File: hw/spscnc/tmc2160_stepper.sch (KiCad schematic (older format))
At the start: 65 parts, among them IC1 TMC2160-TA, Q13 KIA50N06B, Q14 KIA50N06B, Q15 KIA50N06B, Q5 KIA50N06B, Q6 KIA50N06B, Q7 KIA50N06B, Q8 KIA50N06B, Q9 KIA50N06B

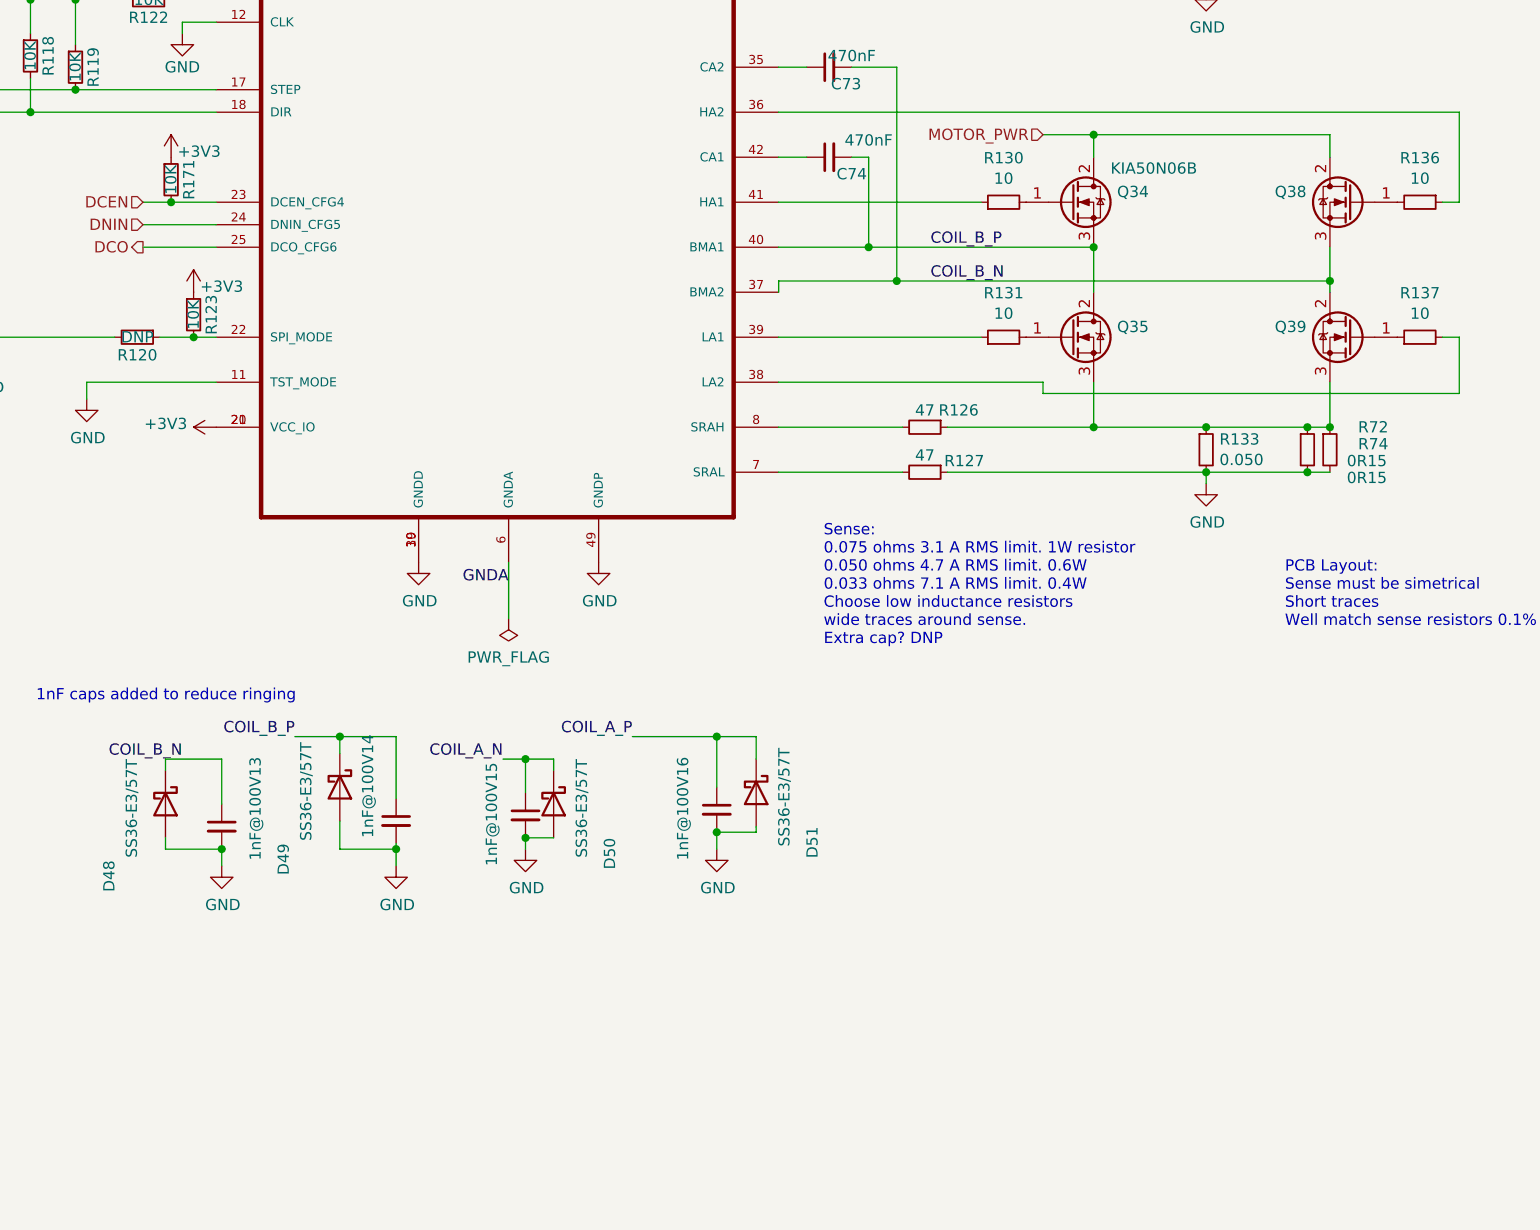
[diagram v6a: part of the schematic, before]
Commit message: Prototype corrections without new PCB
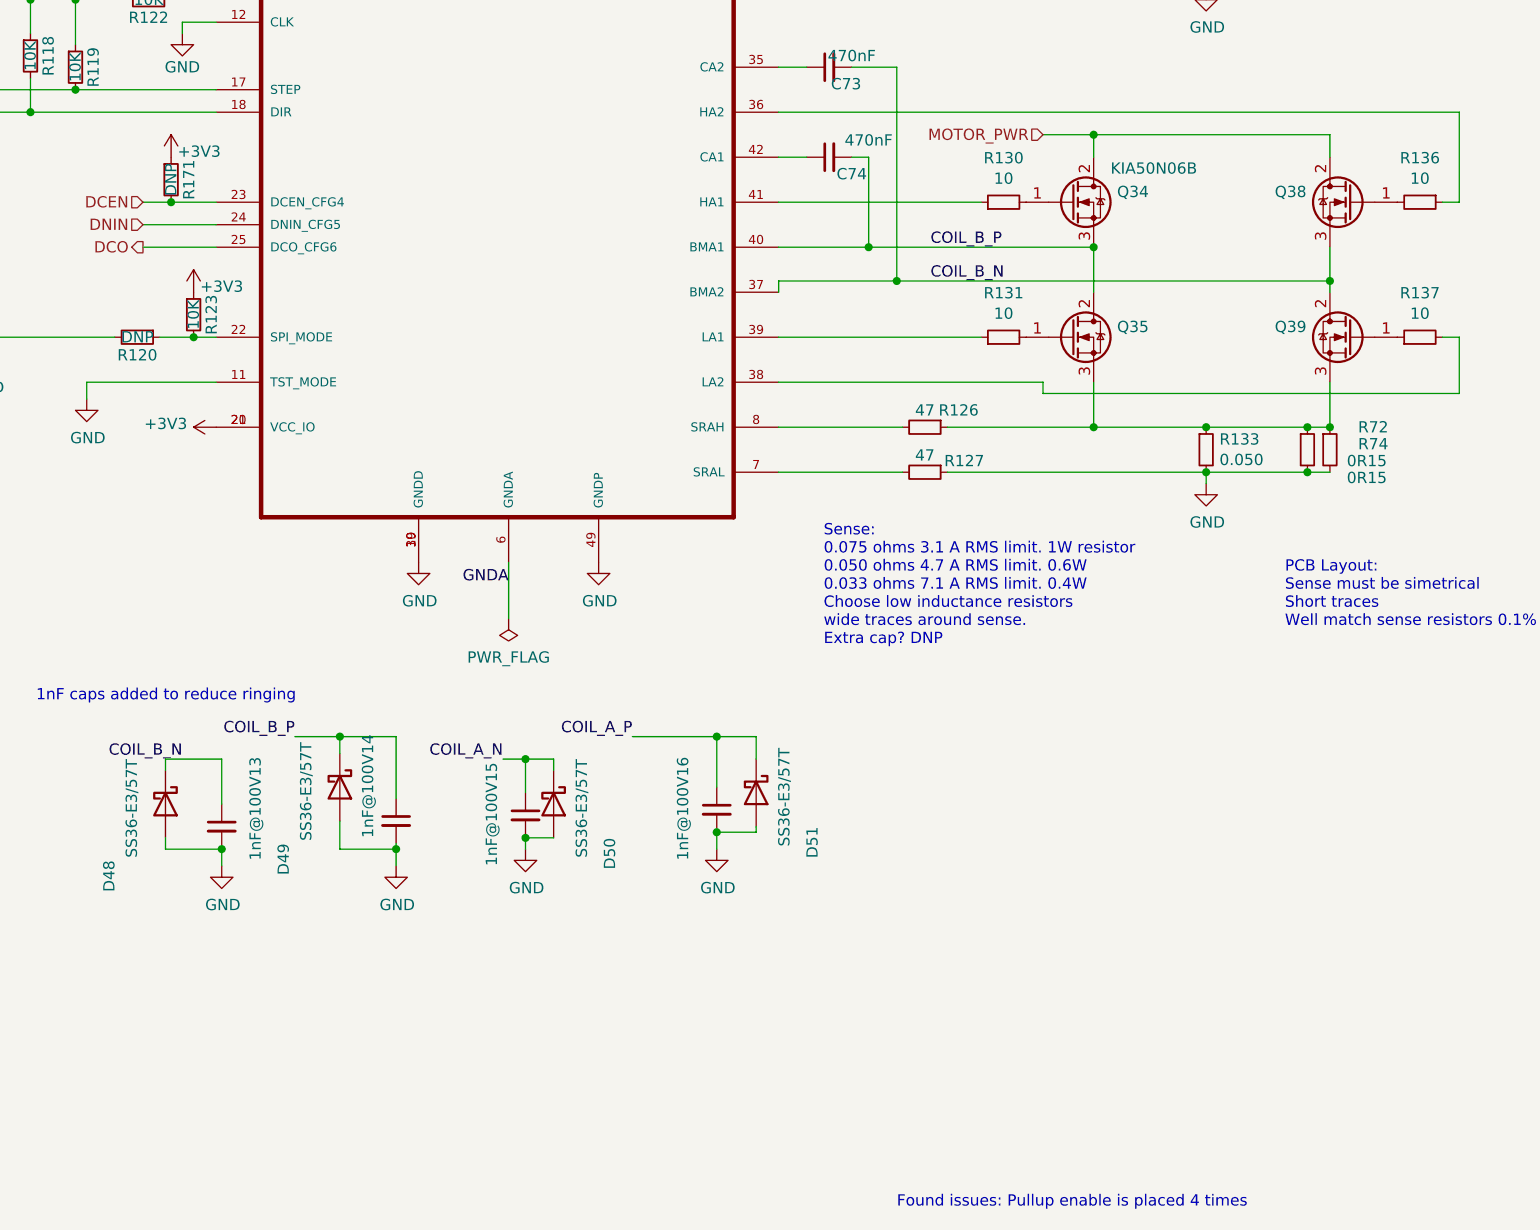
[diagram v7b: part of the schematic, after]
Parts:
- R168: value 10K -> DNP; jlcpcb C17414 -> DNP734
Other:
- note added: "Found issues: Pullup enable is placed 4 times"
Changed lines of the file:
@@
 AR Path="/61E6E495" Ref="#PWR0103"  Part="1"
 AR Path="/6221509B/61E6E495" Ref="#PWR?"  Part="1"
-F 0 "#PWR065" H 1875 1825 50  0001 C CNN
+F 0 "#PWR085" H 1875 1825 50  0001 C CNN
 F 1 "GND" H 1880 1902 50  0000 C CNN
 F 2 "" H 1875 2075 50  0001 C CNN
@@
 AR Path="/61E77854" Ref="#PWR0104"  Part="1"
 AR Path="/6221509B/61E77854" Ref="#PWR?"  Part="1"
-F 0 "#PWR076" H 7050 800 50  0001 C CNN
+F 0 "#PWR096" H 7050 800 50  0001 C CNN
 F 1 "GND" H 7055 877 50  0000 C CNN
 F 2 "" H 7050 1050 50  0001 C CNN
@@
 AR Path="/61E77EC9" Ref="#PWR0105"  Part="1"
 AR Path="/6221509B/61E77EC9" Ref="#PWR?"  Part="1"
-F 0 "#PWR080" H 8525 800 50  0001 C CNN
+F 0 "#PWR0100" H 8525 800 50  0001 C CNN
 F 1 "GND" H 8530 877 50  0000 C CNN
 F 2 "" H 8525 1050 50  0001 C CNN
@@
 AR Path="/6203DFCF/61E7935F" Ref="#PWR091"  Part="1"
 AR Path="/6221509B/61E7935F" Ref="#PWR?"  Part="1"
-F 0 "#PWR071" H 3500 5125 50  0001 C CNN
+F 0 "#PWR091" H 3500 5125 50  0001 C CNN
 F 1 "+3V3" V 3515 5403 50  0000 L CNN
 F 2 "" H 3500 5275 50  0001 C CNN
@@
 AR Path="/61E79E80" Ref="#PWR0110"  Part="1"
 AR Path="/6221509B/61E79E80" Ref="#PWR?"  Part="1"
-F 0 "#PWR064" H 1875 1325 50  0001 C CNN
+F 0 "#PWR084" H 1875 1325 50  0001 C CNN
 F 1 "+12V" H 1890 1648 50  0000 C CNN
 F 2 "" H 1875 1475 50  0001 C CNN
@@
 AR Path="/61E86B21" Ref="#PWR0115"  Part="1"
 AR Path="/6221509B/61E86B21" Ref="#PWR?"  Part="1"
-F 0 "#PWR072" H 4400 5625 50  0001 C CNN
+F 0 "#PWR092" H 4400 5625 50  0001 C CNN
 F 1 "GND" H 4405 5702 50  0000 C CNN
 F 2 "" H 4400 5875 50  0001 C CNN
@@
 AR Path="/61E86EEA" Ref="#PWR0116"  Part="1"
 AR Path="/6221509B/61E86EEA" Ref="#PWR?"  Part="1"
-F 0 "#PWR074" H 5200 5625 50  0001 C CNN
+F 0 "#PWR094" H 5200 5625 50  0001 C CNN
 F 1 "GND" H 5205 5702 50  0000 C CNN
 F 2 "" H 5200 5875 50  0001 C CNN
@@
 AR Path="/6203DFCF/61E89FDE" Ref="#PWR087"  Part="1"
 AR Path="/6221509B/61E89FDE" Ref="#PWR?"  Part="1"
-F 0 "#PWR067" H 2675 3075 50  0001 C CNN
+F 0 "#PWR087" H 2675 3075 50  0001 C CNN
 F 1 "+3V3" H 2690 3398 50  0000 C CNN
 F 2 "" H 2675 3225 50  0001 C CNN
@@
 AR Path="/6203DFCF/61E8CEFE" Ref="#PWR089"  Part="1"
 AR Path="/6221509B/61E8CEFE" Ref="#PWR?"  Part="1"
-F 0 "#PWR069" H 3350 3275 50  0001 C CNN
+F 0 "#PWR089" H 3350 3275 50  0001 C CNN
 F 1 "GND" H 3350 3375 50  0000 C CNN
 F 2 "" H 3350 3525 50  0001 C CNN
@@
 AR Path="/6203DFCF/61EA6B53" Ref="#PWR090"  Part="1"
 AR Path="/6221509B/61EA6B53" Ref="#PWR?"  Part="1"
-F 0 "#PWR070" H 3400 4525 50  0001 C CNN
+F 0 "#PWR090" H 3400 4525 50  0001 C CNN
 F 1 "+3V3" H 3525 4700 50  0000 C CNN
 F 2 "" H 3400 4675 50  0001 C CNN
@@
 AR Path="/61ECB3CC" Ref="#PWR0121"  Part="1"
 AR Path="/6221509B/61ECB3CC" Ref="#PWR?"  Part="1"
-F 0 "#PWR079" H 8075 800 50  0001 C CNN
+F 0 "#PWR099" H 8075 800 50  0001 C CNN
 F 1 "GND" H 8080 877 50  0000 C CNN
 F 2 "" H 8075 1050 50  0001 C CNN
@@
 AR Path="/61F1EBF7" Ref="#PWR0122"  Part="1"
 AR Path="/6221509B/61F1EBF7" Ref="#PWR?"  Part="1"
-F 0 "#PWR077" H 7900 3075 50  0001 C CNN
+F 0 "#PWR097" H 7900 3075 50  0001 C CNN
 F 1 "GND" H 7905 3152 50  0000 C CNN
 F 2 "" H 7900 3325 50  0001 C CNN
@@
 AR Path="/61F26F6F" Ref="#PWR0123"  Part="1"
 AR Path="/6221509B/61F26F6F" Ref="#PWR?"  Part="1"
-F 0 "#PWR068" H 2925 4900 50  0001 C CNN
+F 0 "#PWR088" H 2925 4900 50  0001 C CNN
 F 1 "GND" H 2930 4977 50  0000 C CNN
 F 2 "" H 2925 5150 50  0001 C CNN
@@
 AR Path="/61F3F591" Ref="#PWR0124"  Part="1"
 AR Path="/6221509B/61F3F591" Ref="#PWR?"  Part="1"
-F 0 "#PWR066" H 2475 4675 50  0001 C CNN
+F 0 "#PWR086" H 2475 4675 50  0001 C CNN
 F 1 "GND" H 2480 4752 50  0000 C CNN
 F 2 "" H 2475 4925 50  0001 C CNN
@@
 AR Path="/61F4F366" Ref="#PWR0125"  Part="1"
 AR Path="/6221509B/61F4F366" Ref="#PWR?"  Part="1"
-F 0 "#PWR075" H 10475 5475 50  0001 C CNN
+F 0 "#PWR095" H 10475 5475 50  0001 C CNN
 F 1 "GND" H 10480 5552 50  0000 C CNN
 F 2 "" H 10475 5725 50  0001 C CNN
@@
 AR Path="/61F62E48" Ref="#PWR0126"  Part="1"
 AR Path="/6221509B/61F62E48" Ref="#PWR?"  Part="1"
-F 0 "#PWR081" H 9075 800 50  0001 C CNN
+F 0 "#PWR0120" H 9075 800 50  0001 C CNN
 F 1 "GND" H 9080 877 50  0000 C CNN
 F 2 "" H 9075 1050 50  0001 C CNN
@@
 AR Path="/61F7F4E7" Ref="#PWR0127"  Part="1"
 AR Path="/6221509B/61F7F4E7" Ref="#PWR?"  Part="1"
-F 0 "#PWR078" H 7900 5275 50  0001 C CNN
+F 0 "#PWR098" H 7900 5275 50  0001 C CNN
 F 1 "GND" H 7905 5352 50  0000 C CNN
 F 2 "" H 7900 5525 50  0001 C CNN
@@
 AR Path="/620590A8" Ref="#FLG0110"  Part="1"
 AR Path="/6221509B/620590A8" Ref="#FLG?"  Part="1"
-F 0 "#FLG0112" H 3450 2150 50  0001 C CNN
+F 0 "#FLG0113" H 3450 2150 50  0001 C CNN
 F 1 "PWR_FLAG" H 3450 2248 50  0001 C CNN
 F 2 "" H 3450 2075 50  0001 C CNN
@@
 AR Path="/61FC2A3D" Ref="#PWR03"  Part="1"
 AR Path="/6221509B/61FC2A3D" Ref="#PWR?"  Part="1"
-F 0 "#PWR06" H 10125 5475 50  0001 C CNN
+F 0 "#PWR037" H 10125 5475 50  0001 C CNN
 F 1 "GND" H 10130 5552 50  0000 C CNN
 F 2 "" H 10125 5725 50  0001 C CNN
@@
 AR Path="/6221509B/61F2FC8F" Ref="R?"  Part="1"
 F 0 "R171" V 3380 4175 50  0000 C CNN
-F 1 "10K" V 3300 4175 50  0000 C CNN
+F 1 "DNP" V 3300 4175 50  0000 C CNN
 F 2 "Resistor_SMD:R_0805_2012Metric" V 3230 4175 50  0001 C CNN
 F 3 "" H 3300 4175 50  0001 C CNN
 F 4 "" V 3300 4175 60  0001 C CNN "farnell"
-F 5 "C17414" H 3300 4175 50  0001 C CNN "jlcpcb"
+F 5 "DNP734" H 3300 4175 50  0001 C CNN "jlcpcb"
 F 6 "5%" H 3300 4175 50  0001 C CNN "precision"
 F 7 "1%" H 3300 4175 50  0001 C CNN "power"
@@
 AR Path="/6203DFCF/61F301A3" Ref="#PWR0239"  Part="1"
 AR Path="/6221509B/61F301A3" Ref="#PWR?"  Part="1"
-F 0 "#PWR0238" H 3300 3925 50  0001 C CNN
+F 0 "#PWR0239" H 3300 3925 50  0001 C CNN
 F 1 "+3V3" H 3425 4100 50  0000 C CNN
 F 2 "" H 3300 4075 50  0001 C CNN
@@
 AR Path="/6203DFCF/61F599E0" Ref="#PWR0244"  Part="1"
 AR Path="/6221509B/61F599E0" Ref="#PWR?"  Part="1"
-F 0 "#PWR0242" H 1425 2125 50  0001 C CNN
+F 0 "#PWR0244" H 1425 2125 50  0001 C CNN
 F 1 "+3V3" H 1440 2448 50  0000 C CNN
 F 2 "" H 1425 2275 50  0001 C CNN
@@
 AR Path="/6203DFCF/61F5A3EC" Ref="#PWR0245"  Part="1"
 AR Path="/6221509B/61F5A3EC" Ref="#PWR?"  Part="1"
-F 0 "#PWR0243" H 1050 2200 50  0001 C CNN
+F 0 "#PWR0245" H 1050 2200 50  0001 C CNN
 F 1 "+3V3" H 1065 2523 50  0000 C CNN
 F 2 "" H 1050 2350 50  0001 C CNN
@@
 AR Path="/61FAA995" Ref="#PWR0247"  Part="1"
 AR Path="/6221509B/61FAA995" Ref="#PWR?"  Part="1"
-F 0 "#PWR0255" H 3525 6975 50  0001 C CNN
+F 0 "#PWR0259" H 3525 6975 50  0001 C CNN
 F 1 "GND" H 3530 7052 50  0000 C CNN
 F 2 "" H 3525 7225 50  0001 C CNN
@@
 AR Path="/61FAED05" Ref="#PWR0248"  Part="1"
 AR Path="/6221509B/61FAED05" Ref="#PWR?"  Part="1"
-F 0 "#PWR0256" H 4300 6975 50  0001 C CNN
+F 0 "#PWR0260" H 4300 6975 50  0001 C CNN
 F 1 "GND" H 4305 7052 50  0000 C CNN
 F 2 "" H 4300 7225 50  0001 C CNN
@@
 AR Path="/61FB6882" Ref="#PWR0249"  Part="1"
 AR Path="/6221509B/61FB6882" Ref="#PWR?"  Part="1"
-F 0 "#PWR0257" H 4875 6900 50  0001 C CNN
+F 0 "#PWR0261" H 4875 6900 50  0001 C CNN
 F 1 "GND" H 4880 6977 50  0000 C CNN
 F 2 "" H 4875 7150 50  0001 C CNN
@@
 AR Path="/61FBE4C1" Ref="#PWR0250"  Part="1"
 AR Path="/6221509B/61FBE4C1" Ref="#PWR?"  Part="1"
-F 0 "#PWR0258" H 5725 6900 50  0001 C CNN
+F 0 "#PWR0262" H 5725 6900 50  0001 C CNN
 F 1 "GND" H 5730 6977 50  0000 C CNN
 F 2 "" H 5725 7150 50  0001 C CNN
@@
 AR Path="/61F8983B" Ref="#FLG0104"  Part="1"
 AR Path="/6221509B/61F8983B" Ref="#FLG?"  Part="1"
-F 0 "#FLG0115" H 4800 6200 50  0001 C CNN
+F 0 "#FLG0114" H 4800 6200 50  0001 C CNN
 F 1 "PWR_FLAG" H 4800 6298 50  0000 C CNN
 F 2 "" H 4800 6125 50  0001 C CNN
@@
 Wire Wire Line
 	4800 6125 4800 5875
+Text Notes 6525 8750 0    50   ~ 0
+Found issues: Pullup enable is placed 4 times
 $EndSCHEMATC
